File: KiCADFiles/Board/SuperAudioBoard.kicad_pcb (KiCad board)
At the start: 2 copper layers, 144.5 x 89.2 mm, 176 parts, among them J1 XLR, J2 MONO JACK, J3 Barrel_Jack_PTH, J4 MONO JACK, J5 MONO JACK, J6 MONO JACK, J7 MONO JACK, K2 Fujitsu_FTR-LYCA005x, U1 OPA1655D, U10 OPA1655D, U13 SI8662BC, U14 SI8602AC, U15 OPA1655D, U16 OPA1655D, U17 OPA1655D, U18 OPA1655D, U2 LT1962-3.3, U3 LT1962-5, U4 OPA1655D, U5 CS4272, U6 1512S08-U, U7 Teensy4.0, U8 LT1962, U9 OPA1655D, X1 24.576 MHz 20 pF

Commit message: improved layout further
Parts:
- removed C19: 0.1u, PCM_SparkFun-Capacitor:C_0603_1608Metric
- removed C20: 10u, PCM_SparkFun-Capacitor:C_0805_2012Metric
- removed C47: 22u, Capacitor_THT:CP_Radial_D5.0mm_P2.00mm
- removed RV3, RV4, RV5: 5k, Potentiometer_THT:Potentiometer_Alps_RK163_Single_Horizontal
- added C44: 22u, Capacitor_SMD:C_0805_2012Metric_Pad1.18x1.45mm_HandSolder, F.Cu at (201.5, 79.6)
- added J10: 5k Log Pot, Connector_PinHeader_2.54mm:PinHeader_1x02_P2.54mm_Vertical, F.Cu at (220.6, 118.3)
- added J8: 5k Log Pot, Connector_PinHeader_2.54mm:PinHeader_1x02_P2.54mm_Vertical, F.Cu at (174.7, 116.9)
- added J9: 5k Log Pot, Connector_PinHeader_2.54mm:PinHeader_1x02_P2.54mm_Vertical, F.Cu at (197.7, 116.9)
- C46: footprint Capacitor_THT:CP_Radial_D5.0mm_P2.00mm -> Capacitor_SMD:C_0805_2012Metric_Pad1.18x1.45mm_HandSolder
- U5: footprint Package_SO:TSSOP-28-1EP_4.4x9.7mm_P0.65mm_EP2.74x4.75mm -> Package_SO:TSSOP-28_4.4x9.7mm_P0.65mm
- X1: footprint Crystal:Crystal_SMD_3225-4Pin_3.2x2.5mm_HandSoldering -> Crystal:Crystal_SMD_HC49-SD_HandSoldering
- moved C18 98.0 mm to (203.4, 85.7)
- moved U4 81.7 mm to (209.3, 69.4), turned to 90 degrees
- moved C14 80.7 mm to (206.3, 75.2), turned to -90 degrees
- moved C54 80.6 mm to (206.6, 62.6), turned to 180 degrees
- moved C41 79.7 mm to (205.1, 69.5), turned to 90 degrees
- moved C55 76.3 mm to (206.8, 64.7), turned to 180 degrees
- moved R19 76.1 mm to (208.3, 78.9), turned to 90 degrees
- moved C49 73.6 mm to (212.6, 78.9), turned to -90 degrees
- moved R24 73.0 mm to (208.3, 75.2), turned to 90 degrees
- moved R21 72.9 mm to (210.6, 78.9), turned to 90 degrees
- moved FB8 72.9 mm to (210.1, 64.7), turned to 180 degrees
- moved C45 72.5 mm to (212.8, 73.2), turned to -90 degrees
- moved R25 70.1 mm to (210.6, 75.2), turned to 90 degrees
- moved R29 66.1 mm to (213.6, 76.2)
- moved R27 64.5 mm to (214.8, 70.4), turned to 90 degrees
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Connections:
- net Net-(U5-VD) renamed /CodecAndAnalog/VD_FILT
- C46 pad 1: Net-(C46-Pad1) -> GND
- C46 pad 2: GND -> Net-(C46-Pad2)
- R28 pad 2: Net-(C46-Pad1) -> Net-(C44-Pad2)
- R29 pad 2: Net-(C47-Pad1) -> Net-(C46-Pad2)
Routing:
- net +5VA: track 0.00 -> 116.6 mm, vias 0 -> 2
- net /CodecAndAnalog/InputBufferA/OUT_N: track 5.20 -> 59.0 mm, vias 0 -> 2
- net /CodecAndAnalog/InputBufferB/OUT_N: track 5.20 -> 42.3 mm, vias 0 -> 2
- net /CodecAndAnalog/InputBufferA/OUT_P: track 2.31 -> 35.8 mm
- net /CodecAndAnalog/VCOM: track 0.00 -> 23.8 mm
- net /CodecAndAnalog/MicPreamp/Rg-: track 20.5 -> 0.00 mm
- net /CodecAndAnalog/OutputBufferA/IN_P: track 0.00 -> 16.0 mm
- net /CodecAndAnalog/InputBufferB/OUT_P: track 2.31 -> 17.5 mm
- net +15V: track 42.4 -> 56.4 mm
- net /CodecAndAnalog/OutputBufferA/IN_N: track 0.00 -> 13.4 mm
- net /CodecAndAnalog/OutputBufferB/OUT: track 0.00 -> 12.7 mm
- net Net-(J9-Pin_1): track 16.1 -> 3.66 mm
- net Net-(J8-Pin_1): track 15.4 -> 3.66 mm
- net /CodecAndAnalog/OutputBufferA/OUT: track 0.00 -> 11.6 mm
- net /CodecAndAnalog/InputBufferB/AMP_SIGIN+: track 25.6 -> 14.5 mm
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- added copper zone on F.Cu, net GND
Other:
- board size 144.5 x 89.2 mm -> 87 x 64.4 mm

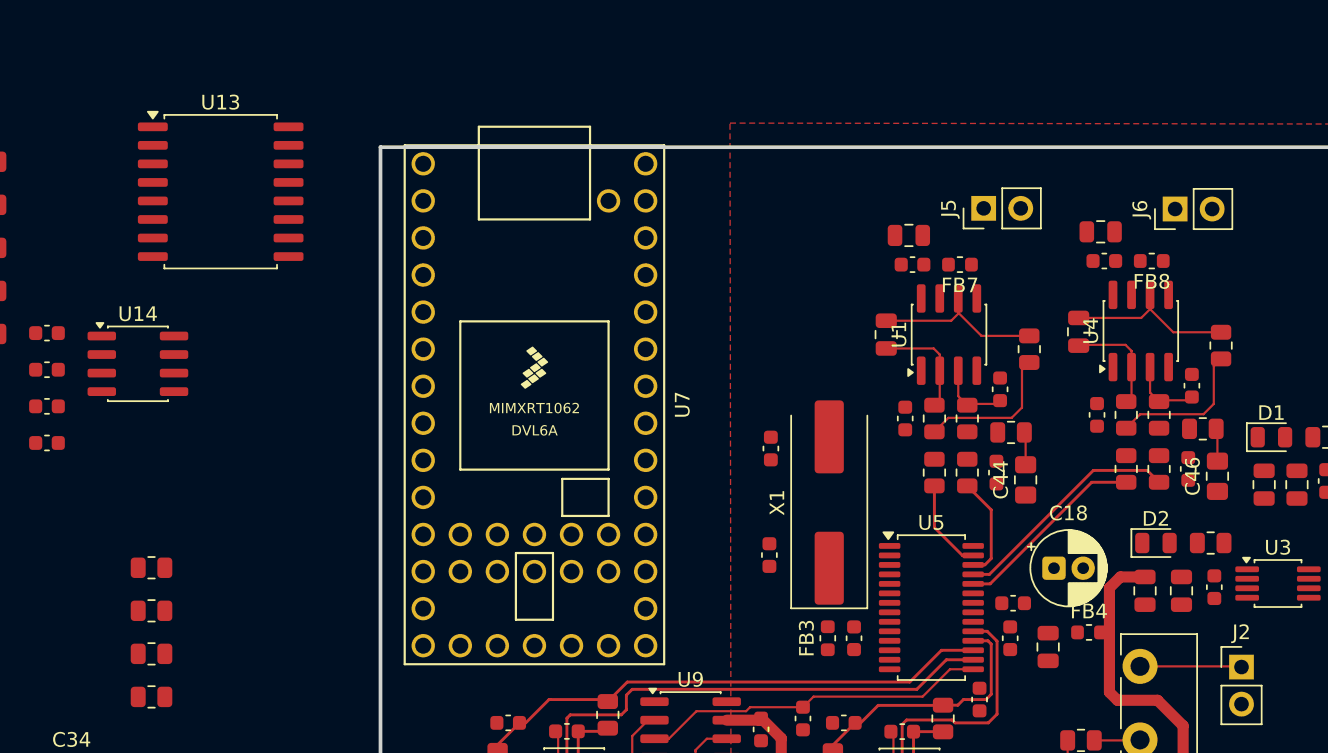
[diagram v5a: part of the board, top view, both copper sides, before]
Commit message: made crystal footprint smaller
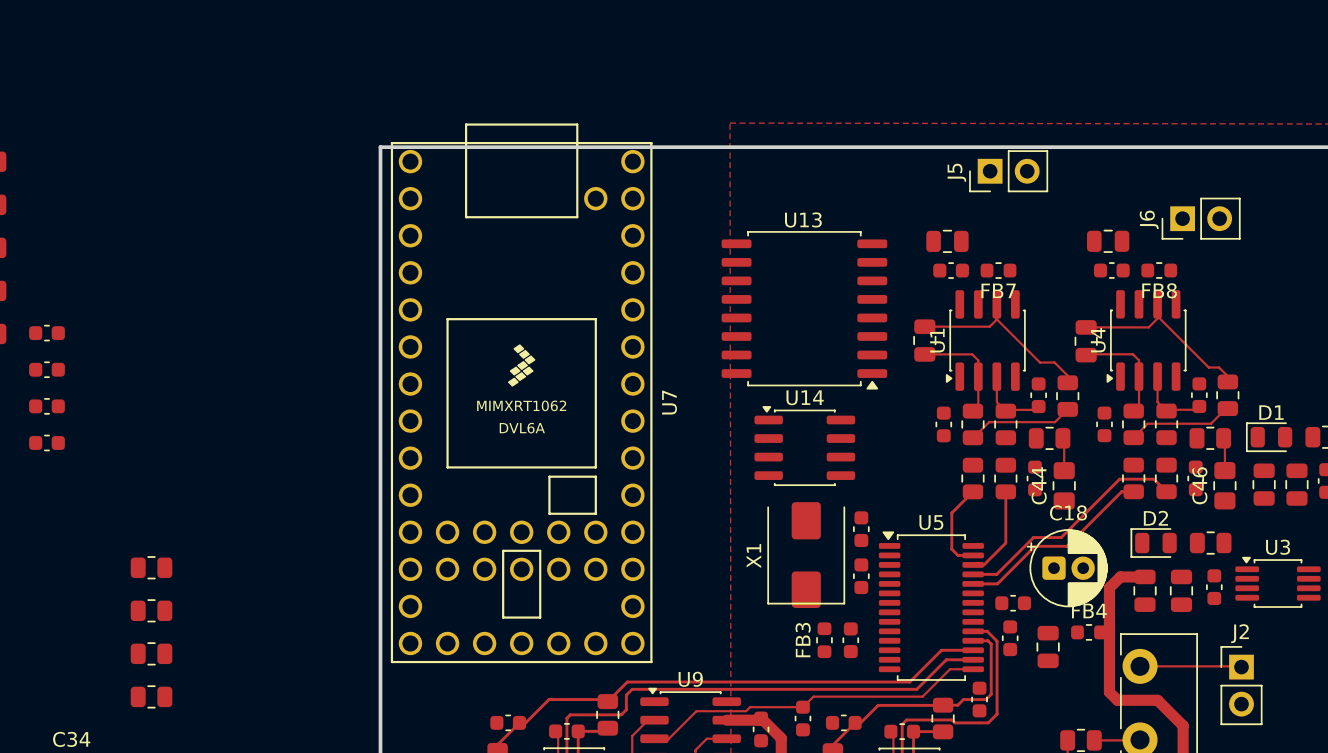
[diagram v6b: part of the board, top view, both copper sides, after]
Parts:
- moved U14 46.1 mm to (186.3, 77.5)
- moved U13 40.8 mm to (186.3, 67.9), turned to 180 degrees
- moved C27 8.30 mm to (190.2, 83.0), turned to -90 degrees
- moved C26 6.46 mm to (190.2, 86.2), turned to 90 degrees
- moved R26 4.16 mm to (204.3, 73.9)
- moved X1 3.95 mm to (186.4, 84.8)
- moved R27 3.44 mm to (215.3, 73.8)
- moved C15 2.67 mm to (194.6, 70.1)
- moved C42 2.67 mm to (202.3, 73.8)
- moved C44 2.67 mm to (204.1, 80.1)
- moved C48 2.67 mm to (202.1, 79.6)
- moved C50 2.67 mm to (196.1, 63.3)
- moved C51 2.67 mm to (196.3, 65.3)
- moved C9 2.67 mm to (195.9, 75.8)
- moved FB7 2.67 mm to (199.6, 65.3)
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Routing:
- net Net-(C14-Pad2): track 9.98 -> 7.28 mm
- net Net-(C9-Pad2): track 9.98 -> 7.30 mm
- net /CodecAndAnalog/OutputBufferA/OUT: track 11.6 -> 13.8 mm
- net /CodecAndAnalog/OutputBufferB/OUT: track 12.7 -> 14.1 mm
- net /CodecAndAnalog/OutputBufferB/IN_P: track 7.08 -> 6.37 mm

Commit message: placed all components, routed most
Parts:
- moved R55 116.5 mm to (238.9, 91.5)
- moved C34 87.1 mm to (215.7, 68.3), turned to 90 degrees
- moved R31 77.5 mm to (214.7, 63.1), turned to 180 degrees
- moved R33 76.1 mm to (210.9, 63.2)
- moved C56 69.1 mm to (191.8, 68.3), turned to 90 degrees
- moved R60 62.5 mm to (184.4, 89.0), turned to -90 degrees
- moved R59 62.2 mm to (186.5, 89.0), turned to -90 degrees
- moved R32 61.7 mm to (196.3, 63.2), turned to 180 degrees
- moved R61 61.6 mm to (189.4, 77.7)
- moved R52 60.5 mm to (179.4, 58.5)
- moved R62 60.4 mm to (189.4, 75.6)
- moved R53 59.7 mm to (179.5, 84.0)
- moved R63 59.6 mm to (189.4, 73.5)
- moved R54 59.4 mm to (179.5, 86.2)
- moved R51 59.3 mm to (179.4, 60.6)
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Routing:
- net /TeensyAndDigital/C_RESET: track 0.00 -> 46.3 mm
- net /TeensyAndDigital/C_DAC_DATA: track 0.00 -> 40.1 mm
- net Net-(U7-8_TX2_IN1): track 0.00 -> 33.7 mm
- net /TeensyAndDigital/T_SCL: track 0.00 -> 26.2 mm, vias 0 -> 4
- net /TeensyAndDigital/T_SDA: track 0.00 -> 24.0 mm
- net /TeensyAndDigital/T_SCLK: track 0.00 -> 20.2 mm, vias 0 -> 2
- net /TeensyAndDigital/C_SDA: track 0.00 -> 18.9 mm, vias 0 -> 2
- net Net-(U7-7_RX2_OUT1A): track 0.00 -> 18.4 mm
- net /CodecAndAnalog/SCLK: track 0.00 -> 17.6 mm, vias 0 -> 2
- net /TeensyAndDigital/C_SCL: track 0.00 -> 17.2 mm
- net /CodecAndAnalog/BCLK: track 0.00 -> 16.3 mm
- net /TeensyAndDigital/T_LRCLK: track 0.00 -> 16.3 mm
- net /TeensyAndDigital/T_3.3V: track 0.00 -> 16.2 mm, vias 0 -> 2
- net /CodecAndAnalog/LRCLK: track 0.00 -> 15.6 mm, vias 0 -> 2
- net /TeensyAndDigital/C_LRCLK: track 0.00 -> 15.4 mm
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- added copper zone on F.Cu, net +3.3V
- added copper zone on B.Cu, net DGND
- added copper zone on F.Cu, net DGND
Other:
- board size 87 x 64.4 mm -> 91.7 x 62.3 mm

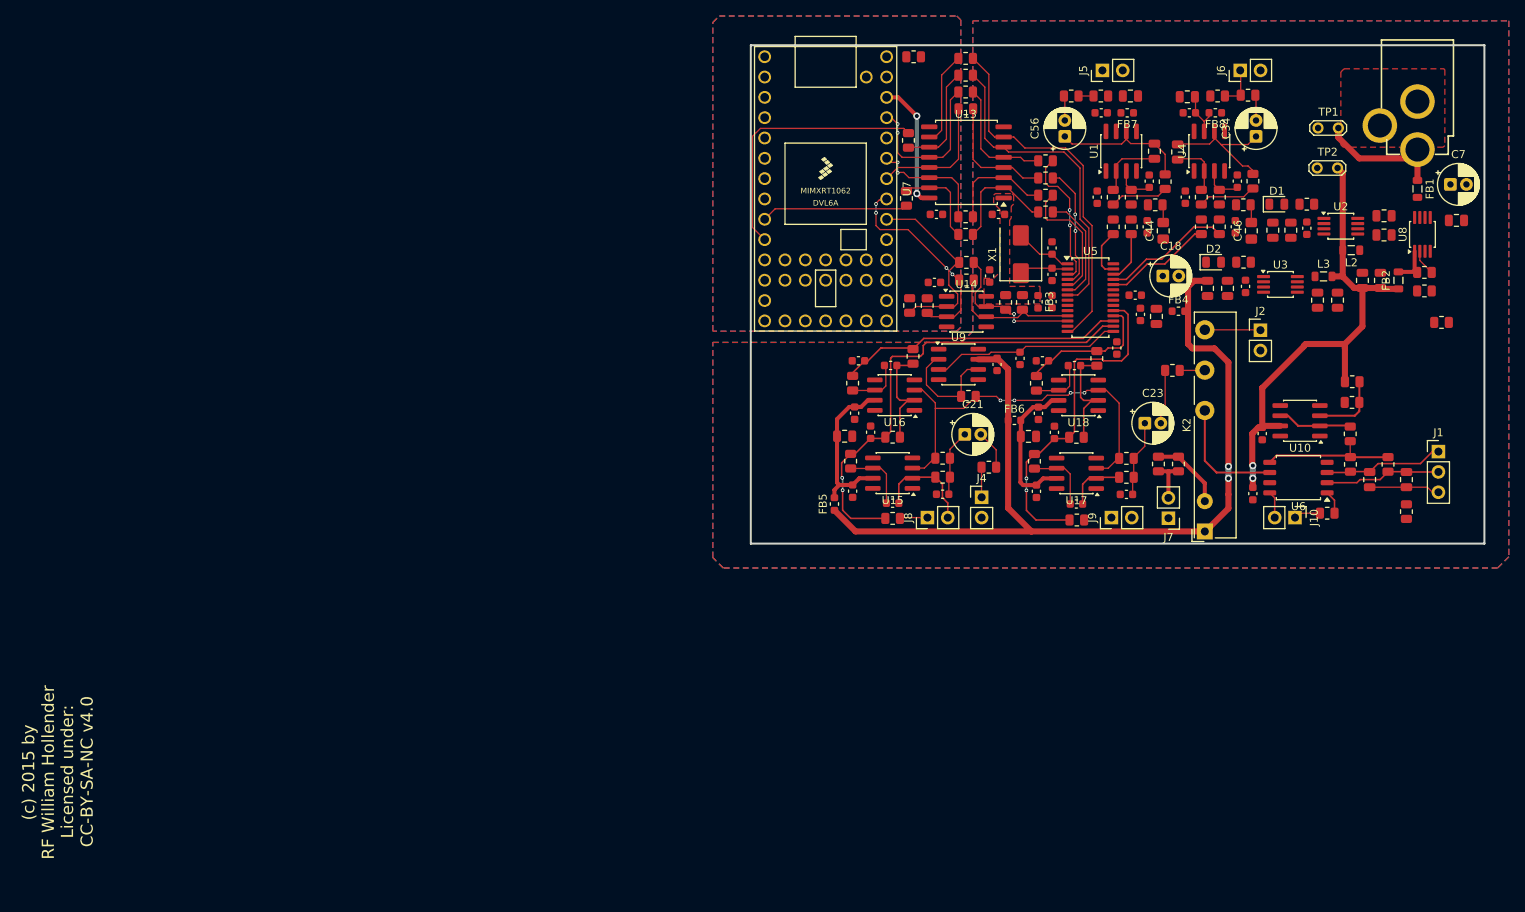
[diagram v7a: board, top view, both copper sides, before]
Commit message: finished layout, passed DRC
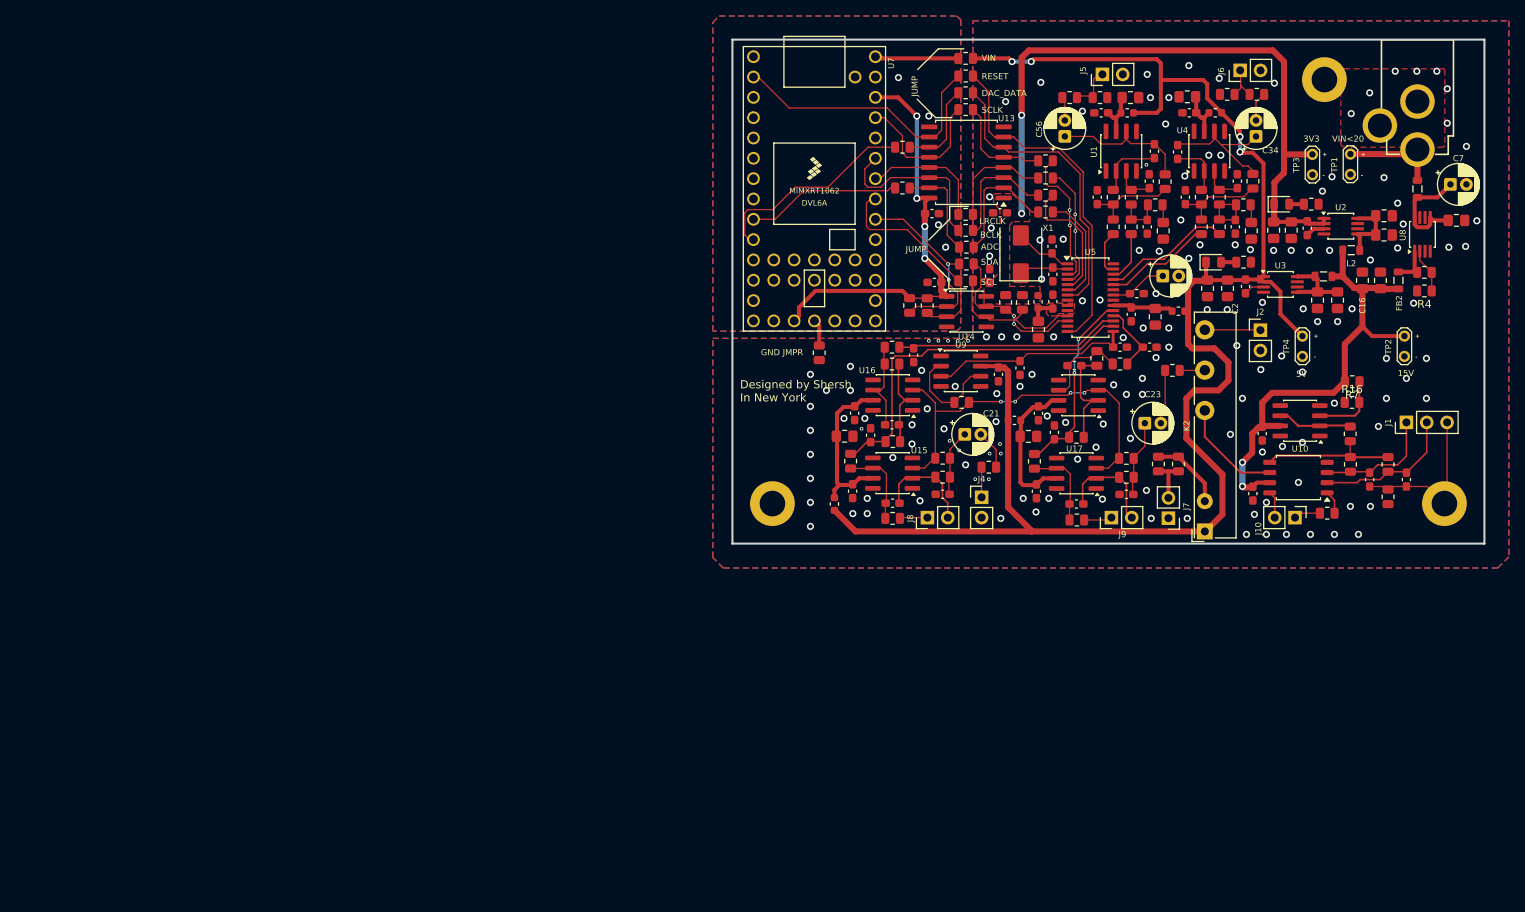
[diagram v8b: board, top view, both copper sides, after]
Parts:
- added C20: 10u, Capacitor_SMD:C_0805_2012Metric_Pad1.18x1.45mm_HandSolder, F.Cu at (188.5, 92.4)
- added H1: MountingHole_Pad, MountingHole:MountingHole_3.2mm_M3_DIN965_Pad, F.Cu at (155.2, 114.2)
- added H2: MountingHole_Pad, MountingHole:MountingHole_3.2mm_M3_DIN965_Pad, F.Cu at (239.2, 114.2)
- added H3: MountingHole_Pad, MountingHole:MountingHole_3.2mm_M3_DIN965_Pad, F.Cu at (224.2, 61.1)
- added TP3: TestPoint_2Pole, TestPoint:TestPoint_2Pads_Pitch2.54mm_Drill0.8mm, F.Cu at (222.8, 73.0)
- added TP4: TestPoint_2Pole, TestPoint:TestPoint_2Pads_Pitch2.54mm_Drill0.8mm, F.Cu at (221.5, 95.8)
- C1, C10, C11, C12, C13, C16, C17, C2, C28, C3, C4, C43, C50, C52, C54, C8: footprint PCM_SparkFun-Capacitor:C_0805_2012Metric -> Capacitor_SMD:C_0805_2012Metric_Pad1.18x1.45mm_HandSolder
- C14, C22, C25, C26, C27, C29, C30, C31, C32, C33, C35, C36, C37, C38, C40, C42, C45, C48, C49, C5, C51, C55, C6, C75, C76, C77, C78, C80, C81, C82, C85, C86, C9, C90, C91, C92, C95, C96: footprint PCM_SparkFun-Capacitor:C_0603_1608Metric -> Capacitor_SMD:C_0603_1608Metric_Pad1.08x0.95mm_HandSolder
- C15, C24, C39, C41: footprint PCM_SparkFun-Capacitor:C_0805_2012Metric -> Capacitor_SMD:C_0603_1608Metric_Pad1.08x0.95mm_HandSolder
- R1, R10, R11, R12, R13, R14, R15, R16, R17, R18, R19, R2, R20, R21, R22, R23, R24, R25, R26, R27, R28, R29, R3, R30, R31, R32, R33, R34, R35, R36, R37, R4, R46, R47, R48, R49, R5, R50, R51, R52, R53, R54, R55, R56, R57, R58, R59, R6, R60, R61, R62, R63, R64, R65, R67, R69, R7, R70, R71, R74, R76, R78, R79, R8, R80, R9: footprint PCM_SparkFun-Resistor:R_0805_2012Metric -> Resistor_SMD:R_0805_2012Metric
- moved R55 77.9 mm to (161.1, 95.3), turned to -90 degrees
- moved TP2 26.0 mm to (234.2, 95.8), turned to 90 degrees
- moved C95 13.5 mm to (202.4, 94.6), turned to 0 degrees
- moved R48 13.2 mm to (179.4, 78.0)
- moved R79 10.7 mm to (198.7, 96.7), turned to 0 degrees
- moved C82 7.42 mm to (170.2, 104.3)
- moved TP1 7.07 mm to (227.5, 73.0), turned to 90 degrees
- moved C85 6.94 mm to (172.9, 95.6), turned to -90 degrees
- moved R70 6.67 mm to (170.2, 94.6), turned to 0 degrees
- moved R46 6.50 mm to (179.4, 58.5)
- moved J1 5.42 mm to (234.5, 104.0), turned to 90 degrees
- moved R5 2.95 mm to (232.2, 113.3)
- moved R69 2.79 mm to (170.2, 96.7), turned to 180 degrees
- moved R47 2.20 mm to (179.4, 64.9)
- moved R52 2.20 mm to (179.4, 60.7)
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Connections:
- R69 pad 2: /CodecAndAnalog/InputBufferA/OUT_P -> Net-(C82-Pad2)
- R78 pad 2: /CodecAndAnalog/InputBufferB/OUT_P -> Net-(C92-Pad2)
- R8 pad 2: /CodecAndAnalog/InputBufferA/OUT_N -> Net-(C81-Pad2)
- R9 pad 2: /CodecAndAnalog/InputBufferB/OUT_N -> Net-(C91-Pad2)
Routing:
- net +5VA: track 111.5 -> 202.5 mm, vias 2 -> 4
- net +3.3V: track 0.00 -> 84.5 mm, vias 0 -> 2
- net /TeensyAndDigital/T_3.3V: track 16.2 -> 53.4 mm, vias 2 -> 4
- net /TeensyAndDigital/T_CODEC_RESET: track 11.8 -> 34.6 mm
- net /CodecAndAnalog/InputBufferB/OUT_N: track 42.6 -> 23.8 mm
- net /PowerSupply/VIN_ANALOG_FILT: track 0.00 -> 13.8 mm
- net /CodecAndAnalog/InputBufferA/OUT_N: track 58.8 -> 45.3 mm, vias 2 -> 0
- net GNDPWR: track 8.86 -> 20.8 mm
- net /TeensyAndDigital/T_VIN: track 0.00 -> 10.5 mm
- net Net-(U3-IN): track 0.00 -> 9.33 mm
- net Net-(U2-IN): track 0.00 -> 9.21 mm
- net /CodecAndAnalog/InputBufferB/OUT_P: track 17.5 -> 8.80 mm
- net Net-(C49-Pad1): track 0.00 -> 7.93 mm
- net Net-(U5-VA): track 0.00 -> 7.65 mm
- net /CodecAndAnalog/InputBufferA/OUT_P: track 35.8 -> 28.3 mm
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- added copper zone on F.Cu, net /CodecAndAnalog/VD_FILT
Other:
- board size 91.7 x 62.3 mm -> 94 x 63 mm
- board text added: "15V"
- board text added: "3V3"
- board text added: "5V"
- board text added: "ADC"
- board text added: "BCLK"
- board text added: "DAC_DATA"
- board text added: "Designed by Shersh In New York"
- board text added: "GND JMPR"
- board text added: "JUMP"
- board text added: "LRCLK"
- board text added: "RESET"
- board text added: "SCL"
- board text added: "SCLK"
- board text added: "SDA"
- board text added: "VIN"
- board text added: "VIN<20"
- board text removed: "(c) 2015 by RF William Hollender"
- board text removed: "(c) 2015 by RF William Hollender (whollender@gmail.com) Licensed under Creative Commons CC-BY-SA-NC v4.0 Not for Commercial Use"
- board text removed: "G"
- board text removed: "I/O Polarity"
- board text removed: "IN A"
- board text removed: "IN B"
- board text removed: "L/R channel determined by CS4272 register settings"
- board text removed: "Licensed under: CC-BY-SA-NC v4.0"
- board text removed: "OUT A"
- board text removed: "OUT B"
- board text removed: "Use mounting lug for chassis ground"
